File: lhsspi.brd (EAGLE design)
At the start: 21.6 x 27.9 mm, 7 parts, among them J1 THUMB, J2 KEYS, J3 HOST, U1 MCP23S17 for SPI

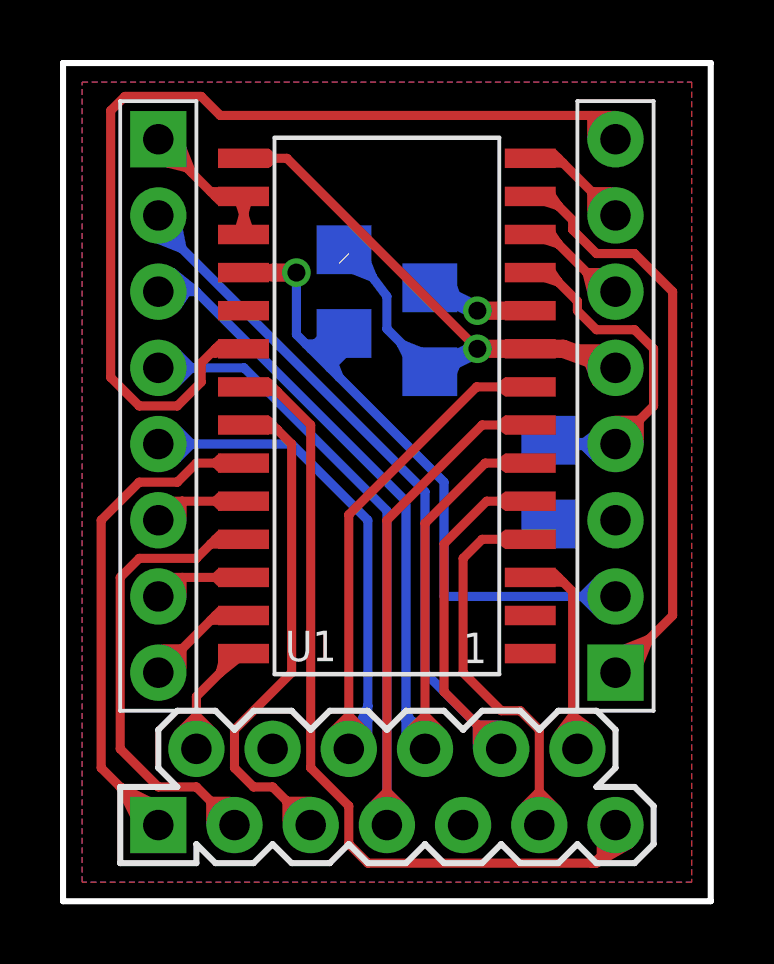
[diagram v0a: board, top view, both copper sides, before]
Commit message: Move R1.
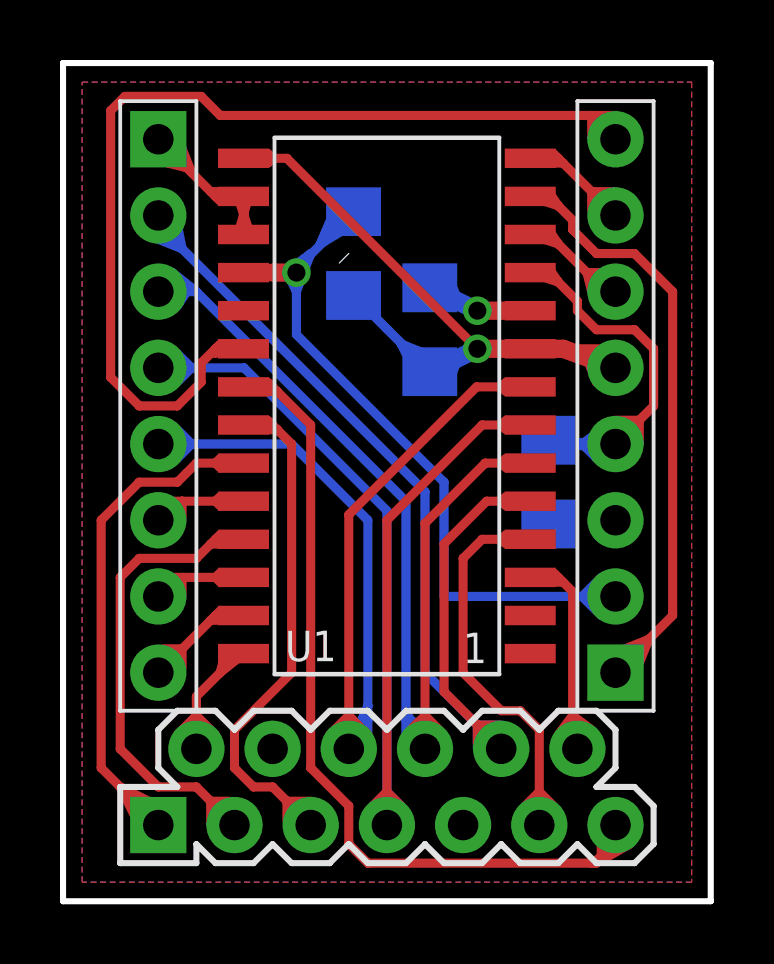
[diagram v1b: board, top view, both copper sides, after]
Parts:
- moved R1 1.31 mm to (9.68, 21.6), turned to 270 degrees
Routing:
- net !RESET: track 25.4 -> 30.9 mm
- net VCC: track 34.4 -> 31.1 mm
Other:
- board text added: "KPS 20130909"
- board text removed: "KPS 20130818"
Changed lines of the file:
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@@
 <setting verticaltext="up"/>
 </settings>
-<grid distance="50" unitdist="mil" unit="mil" style="dots" multiple="1" display="yes" altdistance="12.5" altunitdist="mil" altunit="mil"/>
+<grid distance="50" unitdist="mil" unit="mil" style="dots" multiple="1" display="yes" altdistance="6.25" altunitdist="mil" altunit="mil"/>
 <layers>
 <layer number="1" name="Top" color="4" fill="1" visible="yes" active="yes"/>
@@
 <layer number="20" name="Dimension" color="15" fill="1" visible="yes" active="yes"/>
 <layer number="21" name="tPlace" color="7" fill="1" visible="yes" active="yes"/>
-<layer number="22" name="bPlace" color="14" fill="1" visible="yes" active="yes"/>
+<layer number="22" name="bPlace" color="6" fill="1" visible="yes" active="yes"/>
 <layer number="23" name="tOrigins" color="15" fill="1" visible="yes" active="yes"/>
 <layer number="24" name="bOrigins" color="15" fill="1" visible="yes" active="yes"/>
@@
 <wire x1="0.9525" y1="4.28625" x2="2.2225" y2="4.28625" width="0.1524" layer="22"/>
 <text x="0.79375" y="6.82625" size="0.8128" layer="22" font="vector" rot="MR90">DATA TRAVEL AND EXPERIMENTS</text>
-<text x="20.0025" y="17.78" size="0.8128" layer="22" font="vector" rot="MR90">KPS 20130818</text>
+<text x="20.0025" y="17.78" size="0.8128" layer="22" font="vector" rot="MR90">KPS 20130909</text>
 <text x="4.7625" y="6.985" size="1.6764" layer="22" font="vector" rot="MR90">LEFT
 HAND</text>
@@
 <attribute name="VALUE" x="3.175" y="0" size="1.016" layer="27"/>
 </element>
-<element name="R1" library="misc" package="SMD-1206" value="10K" x="9.36625" y="20.32" smashed="yes" rot="MR90">
-<attribute name="NAME" x="8.79475" y="22.86" size="1.016" layer="26" font="vector" rot="MR90"/>
-<attribute name="VALUE" x="10.38225" y="23.1775" size="0.4064" layer="28" font="vector" rot="MR90" align="bottom-right"/>
+<element name="R1" library="misc" package="SMD-1206" value="10K" x="9.68375" y="21.59" smashed="yes" rot="MR270">
+<attribute name="NAME" x="9.271" y="24.13" size="1.016" layer="26" font="vector" rot="MR90"/>
+<attribute name="VALUE" x="8.66775" y="18.7325" size="0.4064" layer="28" font="vector" rot="MR270" align="bottom-right"/>
 </element>
 <element name="R2" library="misc" package="SMD-1206" value="0Ω" x="16.1925" y="13.97" smashed="yes" rot="MR90">
@@
 <contactref element="R1" pad="2"/>
 <wire x1="12.22375" y1="17.653" x2="12.3825" y2="18.2275" width="0.3048" layer="16"/>
-<wire x1="9.36625" y1="21.717" x2="9.87125" y2="21.24375" width="0.3048" layer="16"/>
-<wire x1="9.87125" y1="21.24375" x2="10.31875" y2="20.79625" width="0.3048" layer="16"/>
-<wire x1="10.31875" y1="20.79625" x2="10.795" y2="20.16125" width="0.3048" layer="16"/>
-<wire x1="10.795" y1="20.16125" x2="10.795" y2="19.07875" width="0.3048" layer="16"/>
 <wire x1="10.795" y1="19.07875" x2="12.2" y2="17.67375" width="0.3048" layer="16"/>
 <wire x1="12.2" y1="17.67375" x2="12.22375" y2="17.653" width="0.3048" layer="16"/>
@@
 <wire x1="16.98625" y1="18.415" x2="18.415" y2="18.415" width="0.3048" layer="1"/>
 <wire x1="18.415" y1="18.415" x2="18.415" y2="17.78" width="0.3048" layer="1"/>
-<wire x1="9.525" y1="21.11375" x2="10.31875" y2="20.79625" width="0.3048" layer="16"/>
-<wire x1="10.31875" y1="20.79625" x2="10.00125" y2="21.59" width="0.3048" layer="16"/>
 <wire x1="13.81125" y1="18.415" x2="13.17625" y2="18.0975" width="0.3048" layer="16"/>
 <wire x1="13.17625" y1="18.0975" x2="12.85875" y2="17.30375" width="0.3048" layer="16"/>
@@
 <wire x1="12.065" y1="18.25625" x2="12.065" y2="17.80875" width="0.3048" layer="16"/>
 <wire x1="12.065" y1="17.80875" x2="12.22375" y2="17.653" width="0.3048" layer="16"/>
+<wire x1="10.795" y1="19.07875" x2="9.68375" y2="20.193" width="0.3048" layer="16"/>
 </signal>
 <signal name="ROW4">
@@
 <via x="7.77875" y="20.955" extent="1-16" drill="0.6"/>
 <wire x1="6.985" y1="20.955" x2="7.77875" y2="20.955" width="0.6096" layer="1"/>
-<wire x1="7.77875" y1="20.955" x2="7.77875" y2="18.89125" width="0.3048" layer="16"/>
+<wire x1="7.77875" y1="20.955" x2="7.77875" y2="20.32" width="0.3048" layer="16"/>
+<wire x1="7.77875" y1="20.32" x2="7.77875" y2="18.89125" width="0.3048" layer="16"/>
 <wire x1="12.7" y1="13.97" x2="12.7" y2="10.16" width="0.3048" layer="16"/>
 <wire x1="12.7" y1="10.16" x2="17.30375" y2="10.16" width="0.3048" layer="16"/>
 <contactref element="R1" pad="1"/>
 <wire x1="17.30375" y1="10.16" x2="18.415" y2="10.16" width="0.3048" layer="16"/>
-<wire x1="9.17875" y1="19.05" x2="9.36625" y2="18.923" width="0.3048" layer="16"/>
-<wire x1="9.3375" y1="18.89125" x2="9.36625" y2="18.923" width="0.3048" layer="16"/>
 <wire x1="17.93875" y1="9.525" x2="17.30375" y2="10.16" width="0.3048" layer="16"/>
 <wire x1="17.30375" y1="10.16" x2="17.93875" y2="10.795" width="0.3048" layer="16"/>
 <wire x1="6.015" y1="20.955" x2="6.985" y2="20.955" width="0.3048" layer="1"/>
-<wire x1="7.77875" y1="18.89125" x2="8.09625" y2="18.57375" width="0.3048" layer="16"/>
-<wire x1="8.09625" y1="18.57375" x2="8.255" y2="18.415" width="0.3048" layer="16"/>
-<wire x1="8.255" y1="18.415" x2="8.89" y2="17.78" width="0.3048" layer="16"/>
-<wire x1="8.89" y1="17.78" x2="9.2075" y2="17.4625" width="0.3048" layer="16"/>
-<wire x1="9.2075" y1="17.4625" x2="12.7" y2="13.97" width="0.3048" layer="16"/>
-<wire x1="9.17875" y1="19.05" x2="8.89" y2="19.05" width="0.3048" layer="16"/>
-<wire x1="8.89" y1="19.05" x2="8.41375" y2="18.57375" width="0.3048" layer="16"/>
-<wire x1="8.41375" y1="18.57375" x2="8.255" y2="18.415" width="0.3048" layer="16"/>
-<wire x1="8.09625" y1="18.57375" x2="8.41375" y2="18.57375" width="0.3048" layer="16"/>
-<wire x1="8.89" y1="17.78" x2="9.36625" y2="18.25625" width="0.3048" layer="16"/>
-<wire x1="9.2075" y1="17.4625" x2="8.89" y2="18.25625" width="0.3048" layer="16"/>
+<wire x1="7.77875" y1="18.89125" x2="12.7" y2="13.97" width="0.3048" layer="16"/>
+<wire x1="7.77875" y1="21.082" x2="9.68375" y2="22.987" width="0.3048" layer="16"/>
+<wire x1="7.77875" y1="20.955" x2="7.77875" y2="21.082" width="0.3048" layer="16"/>
+<wire x1="9.04875" y1="23.01875" x2="8.9666375" y2="22.82715625" width="0.3048" layer="16"/>
+<wire x1="8.9666375" y1="22.82715625" x2="8.5725" y2="21.9075" width="0.3048" layer="16"/>
+<wire x1="8.5725" y1="21.9075" x2="9.36625" y2="22.38375" width="0.3048" layer="16"/>
+<wire x1="9.68375" y1="22.987" x2="9.12648125" y2="22.987" width="0.3048" layer="16"/>
+<wire x1="9.12648125" y1="22.987" x2="8.9666375" y2="22.82715625" width="0.3048" layer="16"/>
+<wire x1="8.255" y1="21.59" x2="7.77875" y2="20.32" width="0.3048" layer="16"/>
+<wire x1="7.77875" y1="20.32" x2="7.46125" y2="20.955" width="0.3048" layer="16"/>
+<wire x1="7.46125" y1="20.955" x2="7.62" y2="21.11375" width="0.3048" layer="16"/>
+<wire x1="7.62" y1="21.11375" x2="8.255" y2="21.59" width="0.3048" layer="16"/>
 </signal>
 <signal name="ROW7">
